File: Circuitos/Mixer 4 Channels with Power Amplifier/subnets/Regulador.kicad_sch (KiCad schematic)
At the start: 12 parts, among them U1 LM7815_TO220, U2 LM7915_TO220

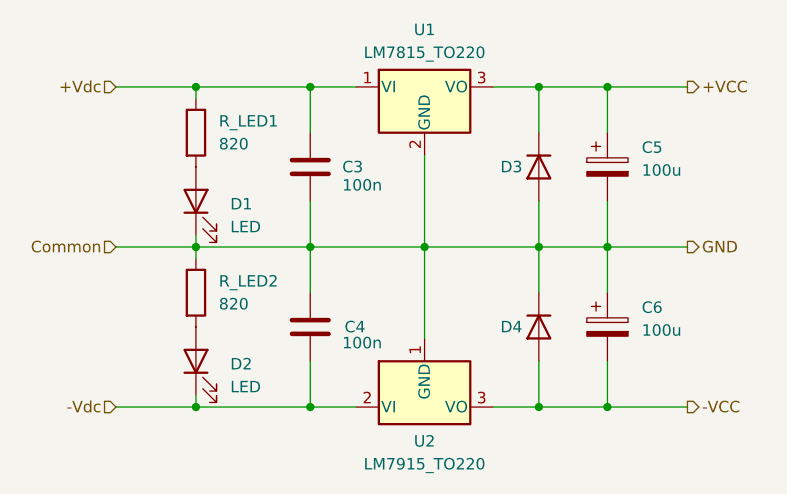
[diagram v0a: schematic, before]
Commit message: Correcciones y modificaciones en fuente, amp auriculares y simul completa
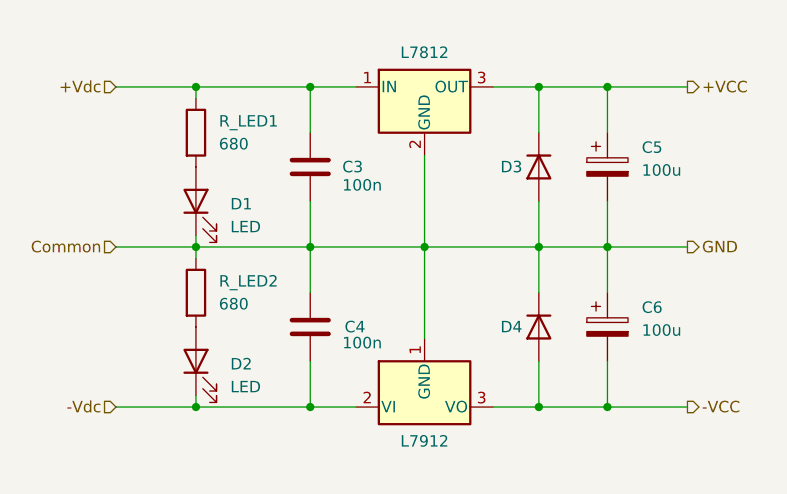
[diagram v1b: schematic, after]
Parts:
- removed U1: LM7815_TO220, Package_TO_SOT_THT:TO-220-3_Vertical, symbol Regulator_Linear:LM7815_TO220
- removed U2: LM7915_TO220, Package_TO_SOT_THT:TO-220-3_Vertical, symbol Regulator_Linear:LM7915_TO220
- added U13: L7812, symbol Regulator_Linear:L7812
- added U14: L7912, symbol Regulator_Linear:L7912
- R_LED1, R_LED2: value 820 -> 680
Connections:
- net +VCC: now also U13.3 (OUT)
- net +Vdc: now also U13.1 (IN)
- net -VCC: now also U14.3 (VO)
- net -Vdc: now also U14.2 (VI)
- net Common: now also U13.2 (GND), U14.1 (GND)
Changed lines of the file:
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@@
 	)
 	(symbol
-		(lib_id "Regulator_Linear:LM7815_TO220")
-		(at 138.43 77.47 0)
+		(lib_id "Regulator_Linear:L7912")
+		(at 138.43 113.03 0)
 		(unit 1)
 		(exclude_from_sim no)
@@
 		(dnp no)
 		(fields_autoplaced yes)
-		(property "Reference" "U1"
-			(at 138.43 71.12 0)
-			(effects
-				(font
-					(size 1.27 1.27)
-				)
-			)
-		)
-		(property "Value" "LM7815_TO220"
-			(at 138.43 73.66 0)
-			(effects
-				(font
-					(size 1.27 1.27)
-				)
-			)
-		)
-		(property "Footprint" "Package_TO_SOT_THT:TO-220-3_Vertical"
-			(at 138.43 71.755 0)
+		(property "Reference" "U14"
+			(at 138.43 116.84 0)
+			(effects
+				(font
+					(size 1.27 1.27)
+				)
+				(hide yes)
+			)
+		)
+		(property "Value" "L7912"
+			(at 138.43 116.84 0)
+			(effects
+				(font
+					(size 1.27 1.27)
+				)
+			)
+		)
+		(property "Footprint" ""
+			(at 138.43 118.11 0)
 			(effects
 				(font
@@
 			)
 		)
-		(property "Datasheet" "https://www.onsemi.cn/PowerSolutions/document/MC7800-D.PDF"
-			(at 138.43 78.74 0)
-			(effects
-				(font
-					(size 1.27 1.27)
-				)
-				(hide yes)
-			)
-		)
-		(property "Description" "Positive 1A 35V Linear Regulator, Fixed Output 15V, TO-220"
-			(at 138.43 77.47 0)
-			(effects
-				(font
-					(size 1.27 1.27)
-				)
-				(hide yes)
-			)
+		(property "Datasheet" "http://www.st.com/content/ccc/resource/technical/document/datasheet/c9/16/86/41/c7/2b/45/f2/CD00000450.pdf/files/CD00000450.pdf/jcr:content/translations/en.CD00000450.pdf"
+			(at 138.43 113.03 0)
+			(effects
+				(font
+					(size 1.27 1.27)
+				)
+				(hide yes)
+			)
+		)
+		(property "Description" "Negative 1.5A 35V Linear Regulator, Fixed Output -12V, TO-220/TO-263"
+			(at 138.43 113.03 0)
+			(effects
+				(font
+					(size 1.27 1.27)
+				)
+				(hide yes)
+			)
+		)
+		(pin "1"
+		)
+		(pin "2"
 		)
 		(pin "3"
 		)
-		(pin "1"
-		)
-		(pin "2"
-		)
-		(instances
-			(project ""
-				(path "/0e2446e7-fd41-47c0-87b8-110c51786f7b/45245042-332e-4026-9c47-78a1402474c5"
-					(reference "U1")
-					(unit 1)
-				)
-			)
-			(project ""
-				(path "/73474962-19a7-474c-a8ee-89a8e49ddff8"
-					(reference "U1")
-					(unit 1)
-				)
-			)
-		)
-	)
-	(symbol
-		(lib_id "Regulator_Linear:LM7915_TO220")
-		(at 138.43 113.03 0)
-		(unit 1)
-		(exclude_from_sim no)
-		(in_bom yes)
-		(on_board yes)
-		(dnp no)
-		(fields_autoplaced yes)
-		(property "Reference" "U2"
-			(at 138.43 116.84 0)
-			(effects
-				(font
-					(size 1.27 1.27)
-				)
-			)
-		)
-		(property "Value" "LM7915_TO220"
-			(at 138.43 119.38 0)
-			(effects
-				(font
-					(size 1.27 1.27)
-				)
-			)
-		)
-		(property "Footprint" "Package_TO_SOT_THT:TO-220-3_Vertical"
-			(at 138.43 118.11 0)
-			(effects
-				(font
-					(size 1.27 1.27)
-					(italic yes)
-				)
-				(hide yes)
-			)
-		)
-		(property "Datasheet" "https://www.onsemi.com/pub/Collateral/MC7900-D.PDF"
-			(at 138.43 113.03 0)
-			(effects
-				(font
-					(size 1.27 1.27)
-				)
-				(hide yes)
-			)
-		)
-		(property "Description" "Negative 1A 35V Linear Regulator, Fixed Output 15V, TO-220"
-			(at 138.43 113.03 0)
-			(effects
-				(font
-					(size 1.27 1.27)
-				)
-				(hide yes)
-			)
-		)
-		(pin "2"
-		)
-		(pin "1"
-		)
-		(pin "3"
-		)
-		(instances
-			(project ""
-				(path "/0e2446e7-fd41-47c0-87b8-110c51786f7b/45245042-332e-4026-9c47-78a1402474c5"
-					(reference "U2")
-					(unit 1)
-				)
-			)
-			(project ""
-				(path "/73474962-19a7-474c-a8ee-89a8e49ddff8"
-					(reference "U2")
+		(instances
+			(project ""
+				(path "/0e2446e7-fd41-47c0-87b8-110c51786f7b/45245042-332e-4026-9c47-78a1402474c5"
+					(reference "U14")
 					(unit 1)
 				)
@@
 			)
 		)
-		(property "Value" "820"
+		(property "Value" "680"
 			(at 115.57 101.5999 0)
 			(effects
@@
 				(path "/73474962-19a7-474c-a8ee-89a8e49ddff8"
 					(reference "C3")
+					(unit 1)
+				)
+			)
+		)
+	)
+	(symbol
+		(lib_id "Regulator_Linear:L7812")
+		(at 138.43 77.47 0)
+		(unit 1)
+		(exclude_from_sim no)
+		(in_bom yes)
+		(on_board yes)
+		(dnp no)
+		(fields_autoplaced yes)
+		(property "Reference" "U13"
+			(at 138.43 71.12 0)
+			(effects
+				(font
+					(size 1.27 1.27)
+				)
+				(hide yes)
+			)
+		)
+		(property "Value" "L7812"
+			(at 138.43 73.66 0)
+			(effects
+				(font
+					(size 1.27 1.27)
+				)
+			)
+		)
+		(property "Footprint" ""
+			(at 139.065 81.28 0)
+			(effects
+				(font
+					(size 1.27 1.27)
+					(italic yes)
+				)
+				(justify left)
+				(hide yes)
+			)
+		)
+		(property "Datasheet" "http://www.st.com/content/ccc/resource/technical/document/datasheet/41/4f/b3/b0/12/d4/47/88/CD00000444.pdf/files/CD00000444.pdf/jcr:content/translations/en.CD00000444.pdf"
+			(at 138.43 78.74 0)
+			(effects
+				(font
+					(size 1.27 1.27)
+				)
+				(hide yes)
+			)
+		)
+		(property "Description" "Positive 1.5A 35V Linear Regulator, Fixed Output 12V, TO-220/TO-263/TO-252"
+			(at 138.43 77.47 0)
+			(effects
+				(font
+					(size 1.27 1.27)
+				)
+				(hide yes)
+			)
+		)
+		(pin "2"
+		)
+		(pin "1"
+		)
+		(pin "3"
+		)
+		(instances
+			(project ""
+				(path "/0e2446e7-fd41-47c0-87b8-110c51786f7b/45245042-332e-4026-9c47-78a1402474c5"
+					(reference "U13")
 					(unit 1)
 				)
@@
 			)
 		)
-		(property "Value" "820"
+		(property "Value" "680"
 			(at 115.57 83.8199 0)
 			(effects

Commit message: Informe finalizado
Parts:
- removed C4: 100n, symbol Device:C
- removed C6: 100u, symbol Device:C_Polarized
- removed D2: LED, symbol Device:LED
- removed D4: D, symbol Device:D
- removed R_LED2: 680, symbol Device:R
- removed U14: L7912, symbol Regulator_Linear:L7912
- renumbered C5 to C11, C3 to C9, D3 to D14, R_LED1 to R_LED3, U13 to U1
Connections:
- net +VCC renamed +VCC2

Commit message: Final de proyecto
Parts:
- renumbered C9 to C?, C11 to C?, D14 to D?, R_LED3 to R_LED?, U1 to U?
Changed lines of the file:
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@@
 		(on_board yes)
 		(dnp no)
-		(property "Reference" "D14"
+		(property "Reference" "D?"
 			(at 148.082 86.36 90)
 			(effects
@@
 		(instances
 			(project "Mixer 4 Channels with Power Amplifier"
+				(path "/0e2446e7-fd41-47c0-87b8-110c51786f7b/45245042-332e-4026-9c47-78a1402474c5"
+					(reference "D?")
+					(unit 1)
+				)
 				(path "/0e2446e7-fd41-47c0-87b8-110c51786f7b/4be8ebac-caad-4f2f-80aa-ca730026f0a1"
 					(reference "D14")
@@
 		(on_board yes)
 		(dnp no)
-		(property "Reference" "C9"
+		(property "Reference" "C?"
 			(at 129.286 86.36 0)
 			(effects
@@
 		(instances
 			(project "Mixer 4 Channels with Power Amplifier"
+				(path "/0e2446e7-fd41-47c0-87b8-110c51786f7b/45245042-332e-4026-9c47-78a1402474c5"
+					(reference "C?")
+					(unit 1)
+				)
 				(path "/0e2446e7-fd41-47c0-87b8-110c51786f7b/4be8ebac-caad-4f2f-80aa-ca730026f0a1"
 					(reference "C9")
@@
 		(dnp no)
 		(fields_autoplaced yes)
-		(property "Reference" "U1"
+		(property "Reference" "U?"
 			(at 138.43 71.12 0)
 			(effects
@@
 		(instances
 			(project "Mixer 4 Channels with Power Amplifier"
+				(path "/0e2446e7-fd41-47c0-87b8-110c51786f7b/45245042-332e-4026-9c47-78a1402474c5"
+					(reference "U?")
+					(unit 1)
+				)
 				(path "/0e2446e7-fd41-47c0-87b8-110c51786f7b/4be8ebac-caad-4f2f-80aa-ca730026f0a1"
 					(reference "U1")
@@
 		(dnp no)
 		(fields_autoplaced yes)
-		(property "Reference" "R_LED3"
+		(property "Reference" "R_LED?"
 			(at 115.57 81.2799 0)
 			(effects
@@
 		(instances
 			(project "Mixer 4 Channels with Power Amplifier"
+				(path "/0e2446e7-fd41-47c0-87b8-110c51786f7b/45245042-332e-4026-9c47-78a1402474c5"
+					(reference "R_LED?")
+					(unit 1)
+				)
 				(path "/0e2446e7-fd41-47c0-87b8-110c51786f7b/4be8ebac-caad-4f2f-80aa-ca730026f0a1"
 					(reference "R_LED3")
@@
 		(on_board yes)
 		(dnp no)
-		(property "Reference" "C11"
+		(property "Reference" "C?"
 			(at 162.56 84.2009 0)
 			(effects
@@
 		(instances
 			(project "Mixer 4 Channels with Power Amplifier"
+				(path "/0e2446e7-fd41-47c0-87b8-110c51786f7b/45245042-332e-4026-9c47-78a1402474c5"
+					(reference "C?")
+					(unit 1)
+				)
 				(path "/0e2446e7-fd41-47c0-87b8-110c51786f7b/4be8ebac-caad-4f2f-80aa-ca730026f0a1"
 					(reference "C11")
